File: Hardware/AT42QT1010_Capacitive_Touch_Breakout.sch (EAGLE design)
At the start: 31 parts, among them Q1 600mA/40V, U1 AT42QT1010 - UDFN

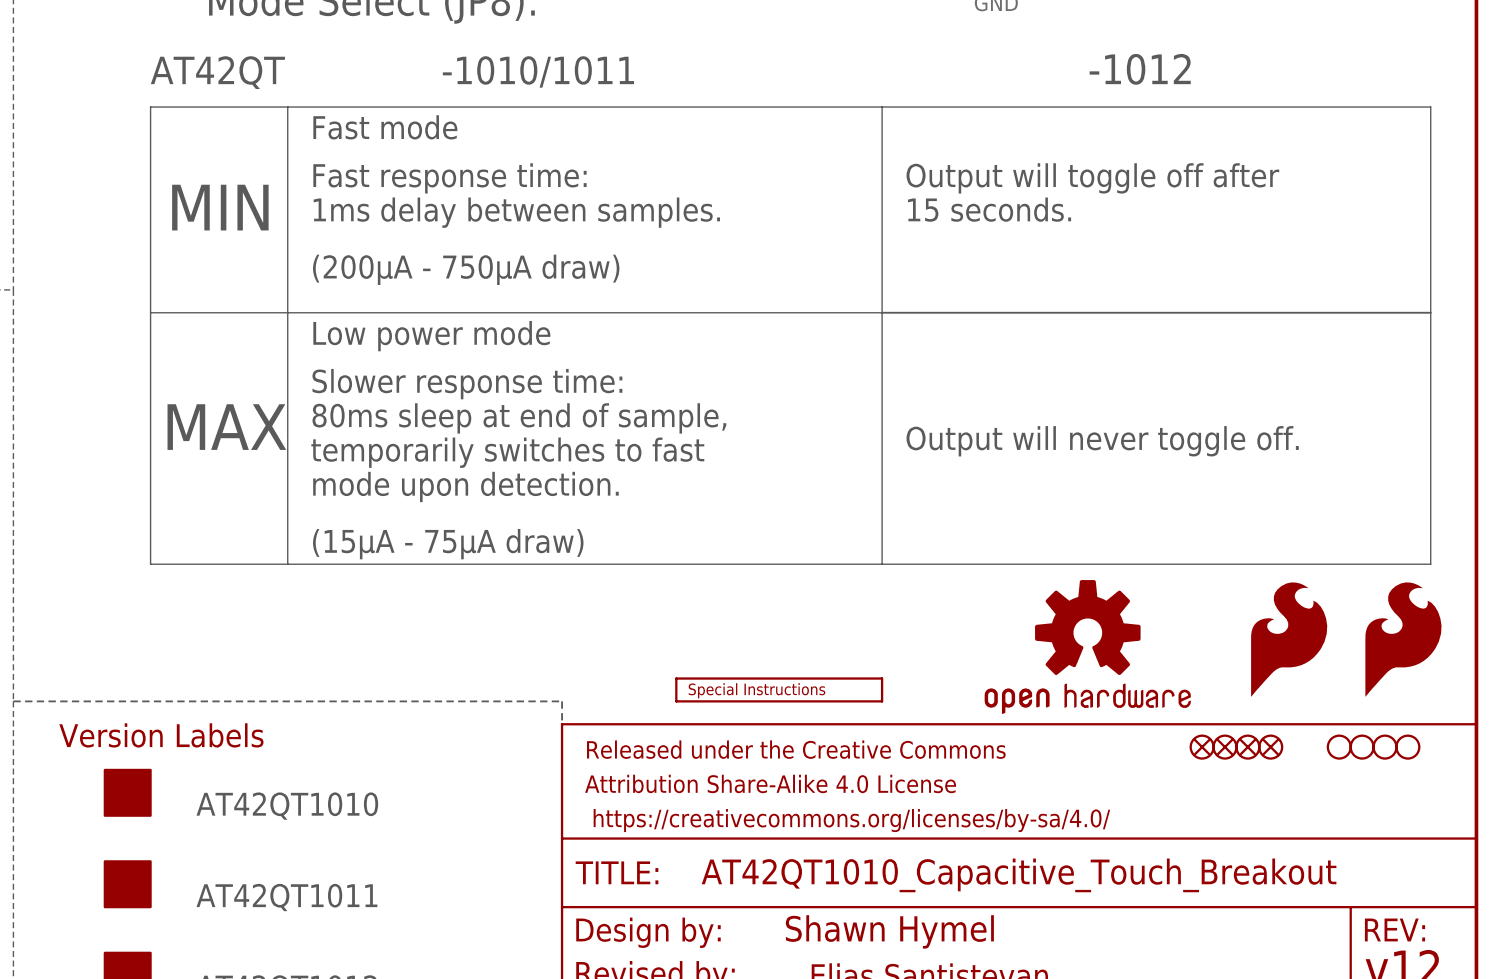
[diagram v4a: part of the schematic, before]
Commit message: Moved silk around.
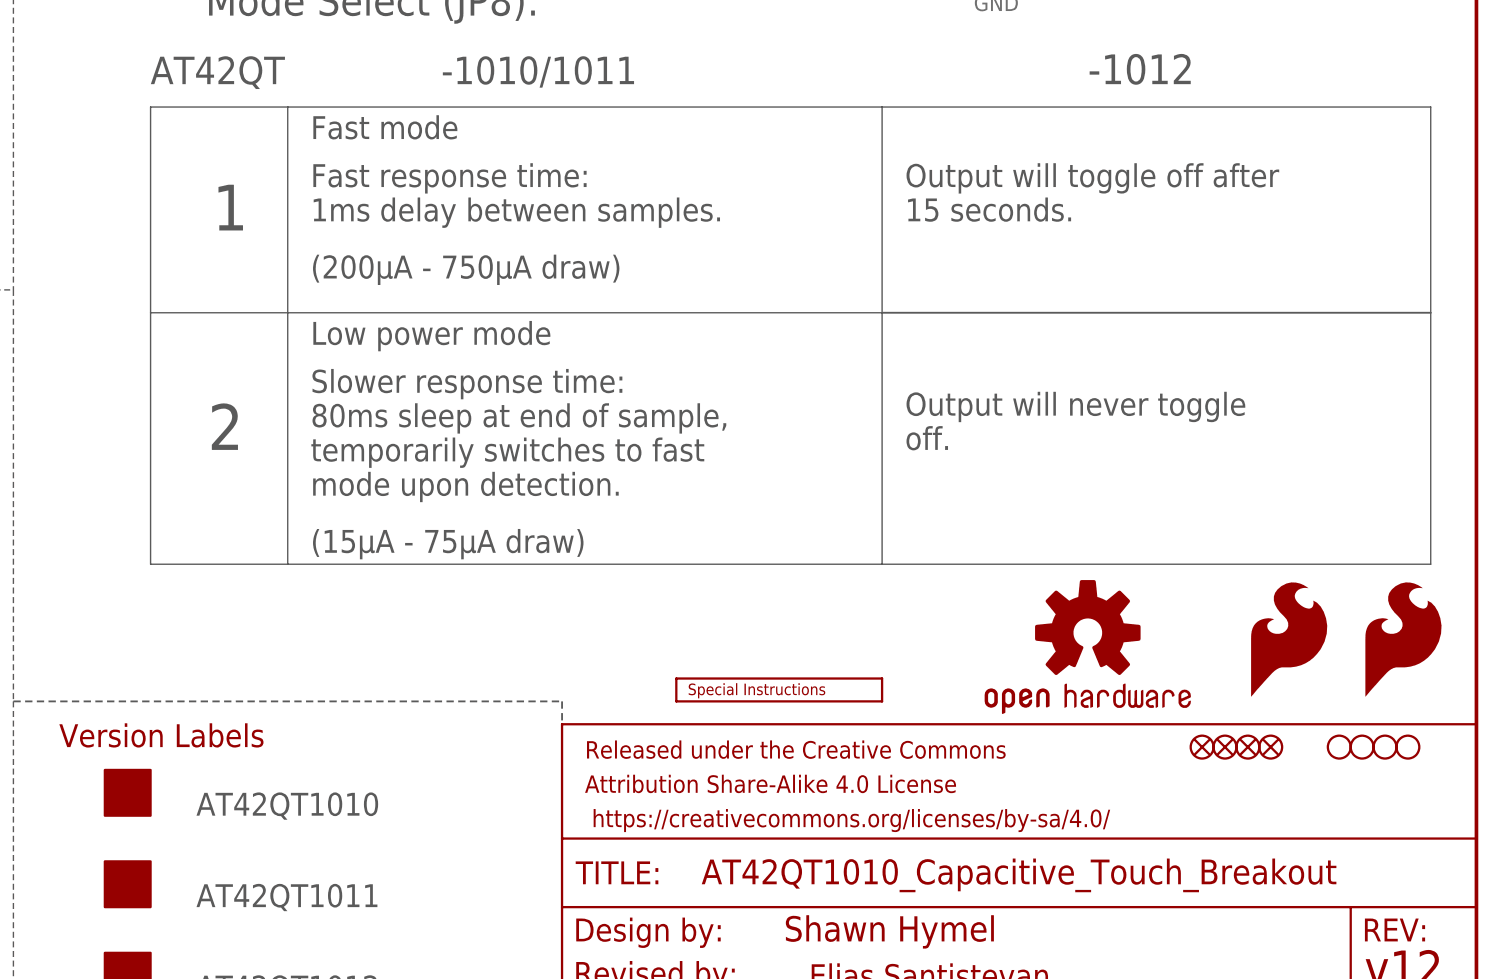
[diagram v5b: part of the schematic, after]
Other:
- note added: "1"
- note added: "2"
- note removed: "MAX"
- note removed: "MIN"
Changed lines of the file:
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@@
 disconnect LED.</text>
 <wire x1="86.36" y1="38.1" x2="147.32" y2="38.1" width="0.2032" layer="97" style="shortdash"/>
-<wire x1="147.32" y1="38.1" x2="147.32" y2="25.4" width="0.2032" layer="97" style="shortdash"/>
 <text x="91.44" y="33.02" size="2.54" layer="94" font="vector">Version Labels</text>
 <text x="106.68" y="25.4" size="2.54" layer="97" font="vector">AT42QT1010</text>
@@
 <text x="185.42" y="91.44" size="2.54" layer="97" font="vector">Output will toggle off after
 15 seconds.</text>
-<text x="185.42" y="66.04" size="2.54" layer="97" font="vector">Output will never toggle off.</text>
+<text x="185.42" y="66.04" size="2.54" layer="97" font="vector">Output will never toggle
+off.</text>
 <wire x1="182.88" y1="81.28" x2="243.84" y2="81.28" width="0.2032" layer="97"/>
-<text x="103.378" y="90.424" size="5.08" layer="97" font="vector" ratio="15">MIN</text>
-<text x="102.87" y="66.04" size="5.08" layer="97" font="vector" ratio="15">MAX</text>
+<text x="108.458" y="90.424" size="5.08" layer="97" font="vector" ratio="15">1</text>
+<text x="107.95" y="66.04" size="5.08" layer="97" font="vector" ratio="15">2</text>
 <text x="205.74" y="106.68" size="3.302" layer="97" font="vector">-1012</text>
 <wire x1="124.46" y1="119.38" x2="124.46" y2="124.46" width="0.2032" layer="97" style="shortdash"/>
 <wire x1="124.46" y1="124.46" x2="193.04" y2="124.46" width="0.2032" layer="97" style="shortdash"/>
 <text x="101.6" y="106.68" size="3.048" layer="97" font="vector">AT42QT </text>
+<wire x1="147.32" y1="38.1" x2="147.32" y2="35.56" width="0.2032" layer="97" style="shortdash"/>
 </plain>
 <instances>

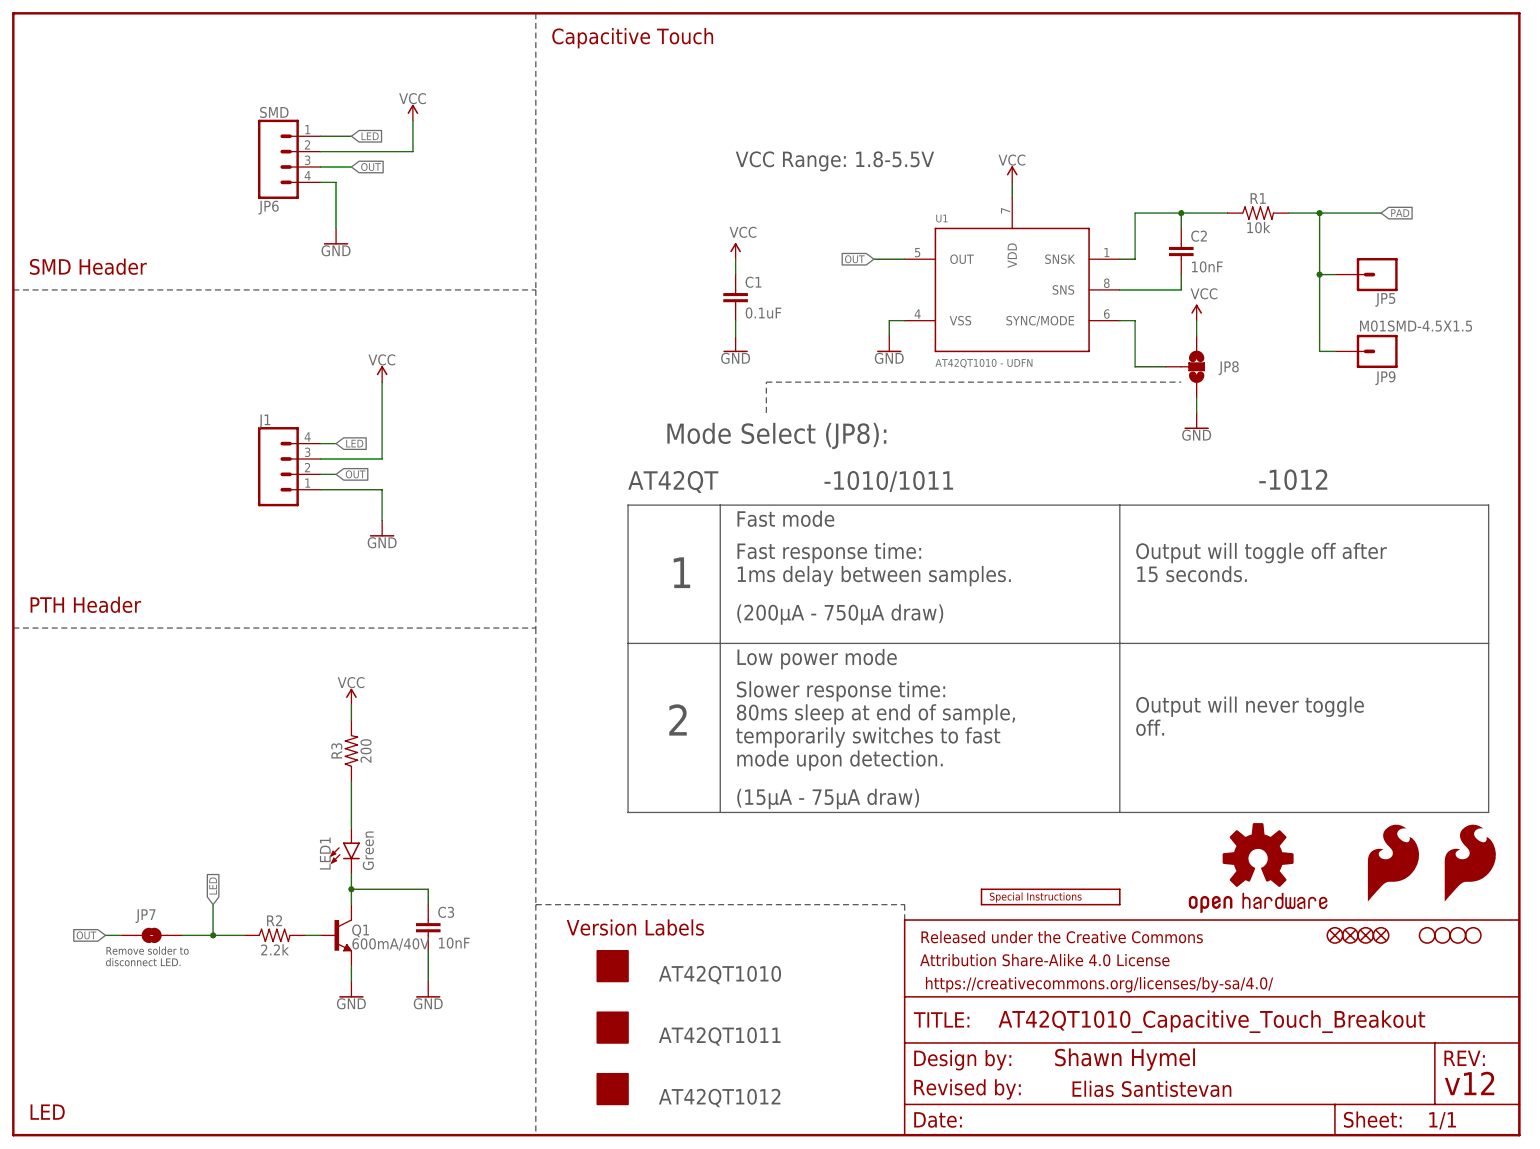
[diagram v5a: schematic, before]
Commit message: Changed blank solder pads to solid slik boxes
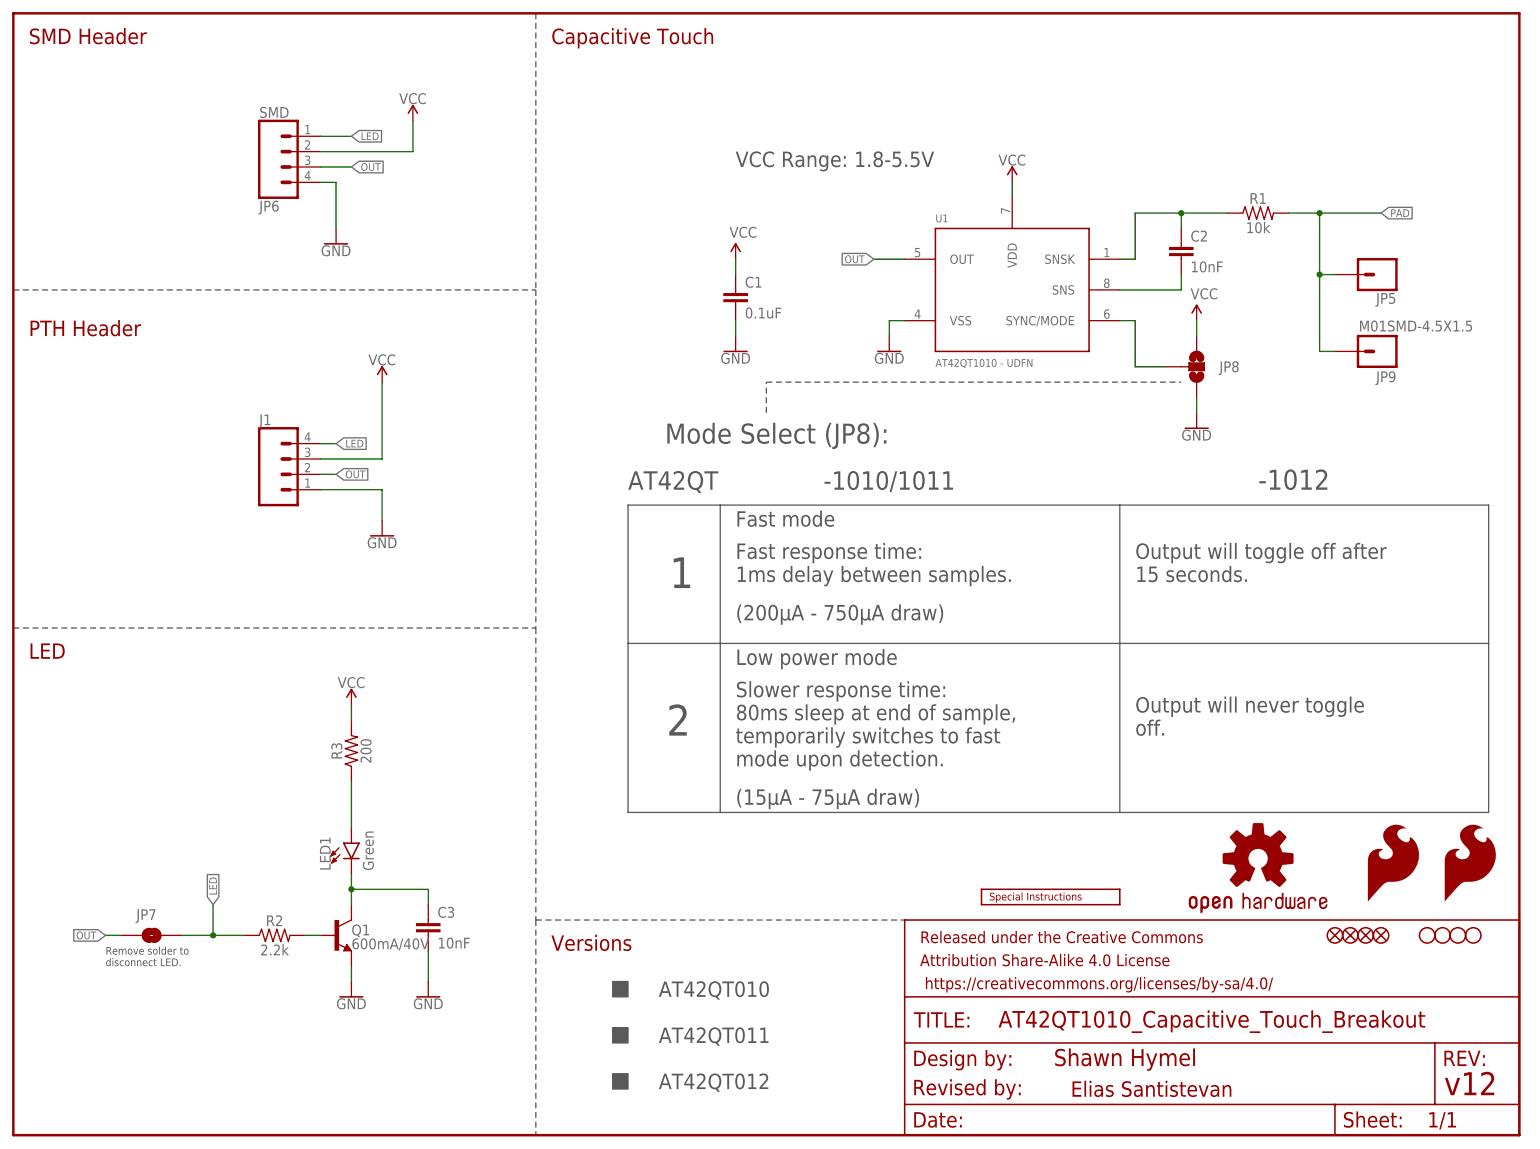
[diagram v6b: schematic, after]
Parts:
- removed U$2, U$3, U$4: SOLDER_PAD_LABEL, local_parts:SOLDER_PAD_LABEL
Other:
- note added: "AT42QT010"
- note added: "AT42QT011"
- note added: "AT42QT012"
- note added: "Versions"
- note removed: "AT42QT1010"
- note removed: "AT42QT1011"
- note removed: "AT42QT1012"
- note removed: "Version Labels"
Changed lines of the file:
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@@
 <part name="LOGO4" library="SparkFun-Aesthetics" deviceset="SFE_LOGO_FLAME" device=".2_INCH"/>
 <part name="LOGO1" library="SparkFun-Aesthetics" deviceset="SFE_LOGO_FLAME" device=".2_INCH"/>
-<part name="U$2" library="local_parts" deviceset="SOLDER_PAD_LABEL" device=""/>
-<part name="U$3" library="local_parts" deviceset="SOLDER_PAD_LABEL" device=""/>
-<part name="U$4" library="local_parts" deviceset="SOLDER_PAD_LABEL" device=""/>
 </parts>
 <sheets>
@@
 <wire x1="86.36" y1="185.42" x2="86.36" y2="139.7" width="0.1524" layer="97" style="shortdash"/>
 <wire x1="86.36" y1="139.7" x2="86.36" y2="83.82" width="0.1524" layer="97" style="shortdash"/>
-<wire x1="86.36" y1="83.82" x2="86.36" y2="38.1" width="0.1524" layer="97" style="shortdash"/>
-<wire x1="86.36" y1="38.1" x2="86.36" y2="0" width="0.1524" layer="97" style="shortdash"/>
+<wire x1="86.36" y1="83.82" x2="86.36" y2="35.56" width="0.1524" layer="97" style="shortdash"/>
+<wire x1="86.36" y1="35.56" x2="86.36" y2="0" width="0.1524" layer="97" style="shortdash"/>
 <wire x1="0" y1="83.82" x2="86.36" y2="83.82" width="0.1524" layer="97" style="shortdash"/>
 <wire x1="0" y1="139.7" x2="86.36" y2="139.7" width="0.1524" layer="97" style="shortdash"/>
 <text x="88.9" y="180.34" size="2.54" layer="94" font="vector">Capacitive Touch</text>
-<text x="2.54" y="142.24" size="2.54" layer="94" font="vector">SMD Header</text>
-<text x="2.54" y="86.36" size="2.54" layer="94" font="vector">PTH Header</text>
-<text x="2.54" y="2.54" size="2.54" layer="94" font="vector">LED</text>
+<text x="2.54" y="180.34" size="2.54" layer="94" font="vector">SMD Header</text>
+<text x="2.54" y="132.08" size="2.54" layer="94" font="vector">PTH Header</text>
+<text x="2.54" y="78.74" size="2.54" layer="94" font="vector">LED</text>
 <text x="144.78" y="106.68" size="3.048" layer="97" font="vector" align="bottom-center">-1010/1011</text>
 <text x="119.38" y="100.584" size="2.54" layer="97" font="vector" ratio="15">Fast mode</text>
@@
 <text x="15.24" y="27.94" size="1.27" layer="97" font="vector">Remove solder to
 disconnect LED.</text>
-<wire x1="86.36" y1="38.1" x2="147.32" y2="38.1" width="0.2032" layer="97" style="shortdash"/>
-<text x="91.44" y="33.02" size="2.54" layer="94" font="vector">Version Labels</text>
-<text x="106.68" y="25.4" size="2.54" layer="97" font="vector">AT42QT1010</text>
-<text x="106.68" y="15.24" size="2.54" layer="97" font="vector">AT42QT1011</text>
-<text x="106.68" y="5.08" size="2.54" layer="97" font="vector">AT42QT1012</text>
-<text x="126.238" y="114.3" size="3.302" layer="97" font="vector" align="bottom-center">Mode Select (JP8):</text>
+<text x="126.238" y="114.3" size="3.302" layer="97" font="vector" ratio="10" align="bottom-center">Mode Select (JP8):</text>
 <wire x1="101.6" y1="104.14" x2="116.84" y2="104.14" width="0.1524" layer="97"/>
 <wire x1="116.84" y1="104.14" x2="182.88" y2="104.14" width="0.1524" layer="97"/>
@@
 <wire x1="124.46" y1="124.46" x2="193.04" y2="124.46" width="0.2032" layer="97" style="shortdash"/>
 <text x="101.6" y="106.68" size="3.048" layer="97" font="vector">AT42QT </text>
-<wire x1="147.32" y1="38.1" x2="147.32" y2="35.56" width="0.2032" layer="97" style="shortdash"/>
+<wire x1="86.36" y1="35.56" x2="147.32" y2="35.56" width="0.2032" layer="97" style="shortdash"/>
+<text x="88.9" y="30.48" size="2.54" layer="94" font="vector">Versions</text>
+<text x="106.68" y="22.86" size="2.54" layer="97" font="vector">AT42QT010</text>
+<text x="106.68" y="15.24" size="2.54" layer="97" font="vector">AT42QT011</text>
+<text x="106.68" y="7.62" size="2.54" layer="97" font="vector">AT42QT012</text>
+<polygon width="0.2032" layer="97">
+<vertex x="99.06" y="25.4"/>
+<vertex x="99.06" y="22.86"/>
+<vertex x="101.6" y="22.86"/>
+<vertex x="101.6" y="25.4"/>
+</polygon>
+<polygon width="0.2032" layer="97">
+<vertex x="99.06" y="17.78"/>
+<vertex x="99.06" y="15.24"/>
+<vertex x="101.6" y="15.24"/>
+<vertex x="101.6" y="17.78"/>
+</polygon>
+<polygon width="0.2032" layer="97">
+<vertex x="99.06" y="10.16"/>
+<vertex x="99.06" y="7.62"/>
+<vertex x="101.6" y="7.62"/>
+<vertex x="101.6" y="10.16"/>
+</polygon>
 </plain>
 <instances>
@@
 <instance part="LOGO4" gate="G$1" x="223.52" y="38.1"/>
 <instance part="LOGO1" gate="G$1" x="236.22" y="38.1"/>
-<instance part="U$2" gate="G$1" x="99.06" y="27.94"/>
-<instance part="U$3" gate="G$1" x="99.06" y="17.78"/>
-<instance part="U$4" gate="G$1" x="99.06" y="7.62"/>
 </instances>
 <busses>

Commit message: Issues from double check Fixed
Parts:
- JP6: device SparkFun-Connectors:CONN_04SMD_LONG -> SparkFun-Connectors:CONN_04SMD
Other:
- note added: "v20"
- note removed: "v12"
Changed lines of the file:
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@@
 <part name="STANDOFF4" library="SparkFun-Hardware" deviceset="STAND-OFF" device=""/>
 <part name="JP5" library="SparkFun-Connectors" deviceset="CONN_01" device=""/>
-<part name="JP6" library="SparkFun-Connectors" deviceset="CONN_04" device="SMD_LONG" value="SMD"/>
+<part name="JP6" library="SparkFun-Connectors" deviceset="CONN_04" device="SMD" value="SMD"/>
 <part name="LED1" library="SparkFun-LED" deviceset="LED-GREEN" device="1206-BOTTOM" value="Green"/>
 <part name="SUPPLY6" library="SparkFun-PowerSymbols" deviceset="VCC" device=""/>
@@
 <plain>
 <text x="171.958" y="11.43" size="2.794" layer="94" font="vector">Shawn Hymel</text>
-<text x="236.474" y="6.604" size="3.81" layer="94" font="vector">v12</text>
+<text x="236.474" y="6.604" size="3.81" layer="94" font="vector">v20</text>
 <wire x1="86.36" y1="185.42" x2="86.36" y2="139.7" width="0.1524" layer="97" style="shortdash"/>
 <wire x1="86.36" y1="139.7" x2="86.36" y2="83.82" width="0.1524" layer="97" style="shortdash"/>
@@
 <vertex x="101.6" y="10.16"/>
 </polygon>
+<text x="200.66" y="119.38" size="3.048" layer="97" font="vector" ratio="15">1</text>
+<text x="200.66" y="132.08" size="3.048" layer="97" font="vector" ratio="15">2</text>
+<wire x1="196.596" y1="120.65" x2="199.898" y2="120.65" width="0.2032" layer="97" style="shortdash"/>
+<wire x1="196.342" y1="133.35" x2="199.898" y2="133.35" width="0.2032" layer="97" style="shortdash"/>
 </plain>
 <instances>
